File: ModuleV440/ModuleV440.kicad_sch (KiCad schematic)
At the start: 42 parts

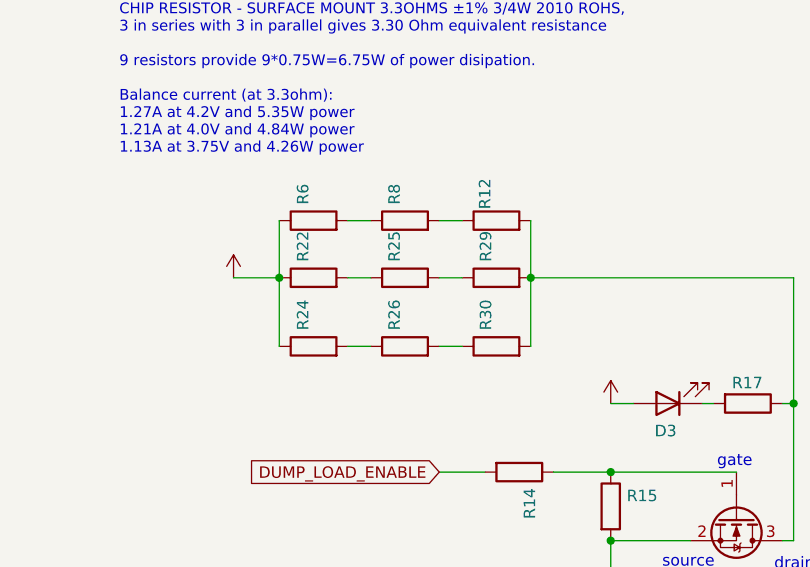
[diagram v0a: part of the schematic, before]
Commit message: V4.4 PCB design update
Changes:

* reconnect a couple of misaligned vias
* move non-power routes (PTC, bypass switch transistor) off the heat dissipation area
* add a lot of vias and copper to resistor array, for improved heat dissipation
* rearranged resistor array for more connections == larger copper area
* moved the slit up a bit for more room in heat dissipation area
* added "not in schematic" tags to the mount holes

Component values and placement have NOT changed.
(Exception: parts of the resistor array have switched places. That's obviously harmless.)
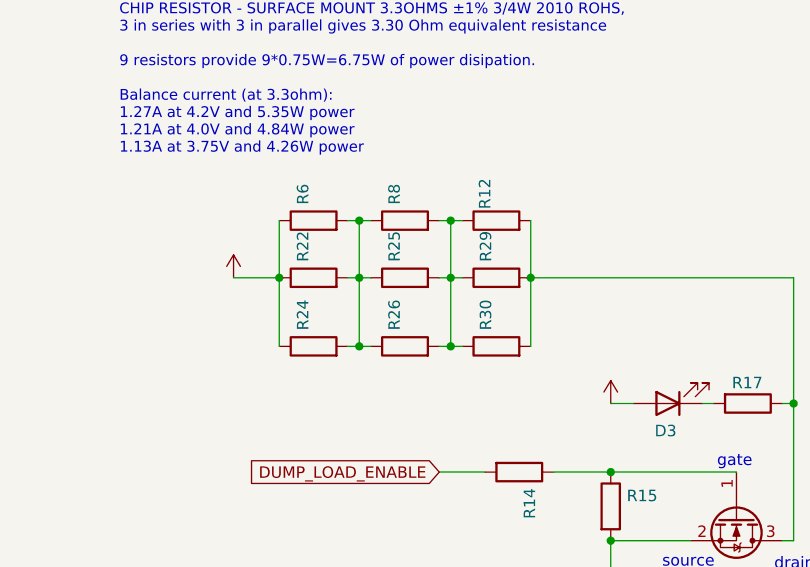
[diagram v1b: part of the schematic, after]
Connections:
- net at R6.2, R8.1: now also R22.2, R24.2, R25.1, R26.1
- net at R12.1, R8.2: now also R25.2, R26.2, R29.1, R30.1
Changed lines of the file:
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@@
     (company "Stuart Pittaway")
   )
+  (junction (at 219.71 59.69) (diameter 0) (color 0 0 0 0)
+  )
+  (junction (at 229.87 67.31) (diameter 0) (color 0 0 0 0)
+  )
   (junction (at 34.29 71.12) (diameter 0) (color 0 0 0 0)
   )
   (junction (at 137.16 172.72) (diameter 0) (color 0 0 0 0)
   )
+  (junction (at 219.71 53.34) (diameter 0) (color 0 0 0 0)
+  )
   (junction (at 100.33 118.11) (diameter 0) (color 0 0 0 0)
   )
   (junction (at 146.05 172.72) (diameter 0) (color 0 0 0 0)
   )
+  (junction (at 229.87 59.69) (diameter 0) (color 0 0 0 0)
+  )
   (junction (at 87.63 60.96) (diameter 0) (color 0 0 0 0)
   )
@@
   (junction (at 243.84 144.78) (diameter 0) (color 0 0 0 0)
   )
+  (junction (at 219.71 67.31) (diameter 0) (color 0 0 0 0)
+  )
   (junction (at 87.63 87.63) (diameter 0) (color 0 0 0 0)
   )
@@
   (junction (at 186.69 143.51) (diameter 0) (color 0 0 0 0)
   )
+  (junction (at 229.87 53.34) (diameter 0) (color 0 0 0 0)
+  )
   (junction (at 102.87 105.41) (diameter 0) (color 0 0 0 0)
   )
@@
     (stroke (width 0) (type default) (color 0 0 0 0))
   )
+  (wire (pts (xy 219.71 67.31) (xy 220.98 67.31))
+    (stroke (width 0) (type default) (color 0 0 0 0))
+  )
   (wire (pts (xy 259.08 124.46) (xy 259.08 123.19))
     (stroke (width 0) (type default) (color 0 0 0 0))
@@
     (stroke (width 0) (type default) (color 0 0 0 0))
   )
+  (wire (pts (xy 219.71 53.34) (xy 220.98 53.34))
+    (stroke (width 0) (type default) (color 0 0 0 0))
+  )
   (wire (pts (xy 146.05 172.72) (xy 157.48 172.72))
     (stroke (width 0) (type default) (color 0 0 0 0))
   )
-  (wire (pts (xy 218.44 53.34) (xy 220.98 53.34))
+  (wire (pts (xy 218.44 53.34) (xy 219.71 53.34))
     (stroke (width 0) (type default) (color 0 0 0 0))
   )
@@
     (stroke (width 0) (type default) (color 0 0 0 0))
   )
+  (wire (pts (xy 229.87 59.69) (xy 229.87 67.31))
+    (stroke (width 0) (type default) (color 0 0 0 0))
+  )
   (wire (pts (xy 210.82 53.34) (xy 210.82 59.69))
     (stroke (width 0) (type default) (color 0 0 0 0))
@@
     (stroke (width 0) (type default) (color 0 0 0 0))
   )
-  (wire (pts (xy 218.44 59.69) (xy 220.98 59.69))
+  (wire (pts (xy 218.44 59.69) (xy 219.71 59.69))
     (stroke (width 0) (type default) (color 0 0 0 0))
   )
@@
     (stroke (width 0) (type default) (color 0 0 0 0))
   )
+  (wire (pts (xy 229.87 53.34) (xy 231.14 53.34))
+    (stroke (width 0) (type default) (color 0 0 0 0))
+  )
   (polyline (pts (xy 214.376 109.855) (xy 214.376 163.703))
     (stroke (width 0) (type default) (color 0 0 0 0))
@@
     (stroke (width 0) (type default) (color 0 0 0 0))
   )
+  (wire (pts (xy 219.71 59.69) (xy 220.98 59.69))
+    (stroke (width 0) (type default) (color 0 0 0 0))
+  )
   (wire (pts (xy 185.42 137.16) (xy 186.69 137.16))
     (stroke (width 0) (type default) (color 0 0 0 0))
@@
     (stroke (width 0) (type default) (color 0 0 0 0))
   )
+  (wire (pts (xy 229.87 53.34) (xy 229.87 59.69))
+    (stroke (width 0) (type default) (color 0 0 0 0))
+  )
   (wire (pts (xy 173.99 132.08) (xy 179.07 132.08))
     (stroke (width 0) (type default) (color 0 0 0 0))
@@
     (stroke (width 0) (type default) (color 0 0 0 0))
   )
-  (wire (pts (xy 228.6 53.34) (xy 231.14 53.34))
+  (wire (pts (xy 228.6 53.34) (xy 229.87 53.34))
     (stroke (width 0) (type default) (color 0 0 0 0))
   )
@@
     (stroke (width 0) (type default) (color 0 0 0 0))
   )
-  (wire (pts (xy 228.6 59.69) (xy 231.14 59.69))
+  (wire (pts (xy 228.6 59.69) (xy 229.87 59.69))
+    (stroke (width 0) (type default) (color 0 0 0 0))
+  )
+  (wire (pts (xy 219.71 59.69) (xy 219.71 67.31))
+    (stroke (width 0) (type default) (color 0 0 0 0))
+  )
+  (wire (pts (xy 219.71 53.34) (xy 219.71 59.69))
     (stroke (width 0) (type default) (color 0 0 0 0))
   )
@@
     (stroke (width 0) (type default) (color 0 0 0 0))
   )
-  (wire (pts (xy 228.6 67.31) (xy 231.14 67.31))
+  (wire (pts (xy 228.6 67.31) (xy 229.87 67.31))
     (stroke (width 0) (type default) (color 0 0 0 0))
   )
@@
     (stroke (width 0) (type default) (color 0 0 0 0))
   )
+  (wire (pts (xy 229.87 67.31) (xy 231.14 67.31))
+    (stroke (width 0) (type default) (color 0 0 0 0))
+  )
   (wire (pts (xy 22.86 59.69) (xy 22.86 57.15))
     (stroke (width 0) (type default) (color 0 0 0 0))
@@
     (stroke (width 0) (type default) (color 0 0 0 0))
   )
-  (wire (pts (xy 218.44 67.31) (xy 220.98 67.31))
+  (wire (pts (xy 218.44 67.31) (xy 219.71 67.31))
     (stroke (width 0) (type default) (color 0 0 0 0))
   )
@@
     (stroke (width 0) (type default) (color 0 0 0 0))
   )
+  (wire (pts (xy 229.87 59.69) (xy 231.14 59.69))
+    (stroke (width 0) (type default) (color 0 0 0 0))
+  )
